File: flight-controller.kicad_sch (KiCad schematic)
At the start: 66 parts, among them J1 USB_C_Receptacle_USB2.0, Q1 AO3400A, SW1 SW_Push, U1 AT32F435RGT7, U2 BMI270, U3 BMP280, U4 W25N01GVZEIG, U5 AT7456E, U6 TPS54302, U7 TPS54302, U8 TLV75733PDBV, U9 USBLC6-2P6, Y1 27MHz

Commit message: Update notes and TODO items
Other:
- note added: "NOTES * TMR3 pins are for primary motors. * TMR3 pins could be mapped to TMR8. * TMR2/TMR9 are for servos. * Consider TagConnect for SWD * Some capacitors may be redundant depending on layout."
- note added: "TODO * Voltage sense * Pads * Connectors * LED resistors * OSD crystal"
- note removed: "NOTES * TMR3 pins are for primary motors. * TMR3 pins could be mapped to TMR8. * TMR2/TMR9 are for servos. * Confirm that crystal is not needed for USB. * Check we can interrupt on PB0 * LED supplies can be 5V as long as LED pins on MCU are FT. * Consider TagConnect for SWD"
- note removed: "TODO * Voltage sense * Current sense * Pads * Connectors"
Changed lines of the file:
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@@
     (effects (font (size 1.27 1.27)) (justify left bottom))
   )
-  (text "TODO\n* Voltage sense\n* Current sense\n* Pads\n* Connectors"
+  (text "TODO\n* Voltage sense\n* Pads\n* Connectors\n* LED resistors\n* OSD crystal"
     (at 264.16 109.22 0)
     (effects (font (size 1.27 1.27)) (justify left bottom))
   )
-  (text "NOTES\n* TMR3 pins are for primary motors.\n* TMR3 pins could be mapped to TMR8.\n* TMR2/TMR9 are for servos.\n* Confirm that crystal is not needed\n  for USB.\n* Check we can interrupt on PB0\n* LED supplies can be 5V as long as\n  LED pins on MCU are FT.\n* Consider TagConnect for SWD"
+  (text "NOTES\n* TMR3 pins are for primary motors.\n* TMR3 pins could be mapped to TMR8.\n* TMR2/TMR9 are for servos.\n* Consider TagConnect for SWD\n* Some capacitors may be redundant\n  depending on layout."
     (at 223.52 109.22 0)
     (effects (font (size 1.27 1.27)) (justify left bottom))

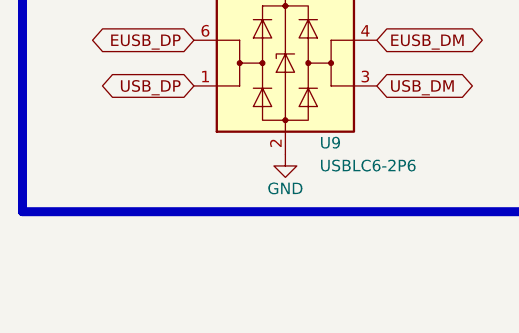
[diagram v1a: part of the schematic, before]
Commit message: Add 3D model for USB C, add speculative board and pad shapes
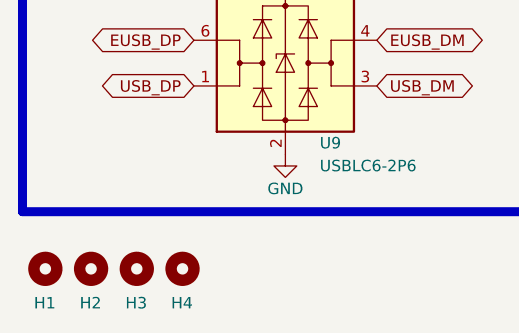
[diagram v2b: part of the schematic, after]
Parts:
- added H1, H2, H3, H4: MountingHole, MountingHole:MountingHole_3.2mm_M3, symbol Mechanical:MountingHole
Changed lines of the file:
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@@
+    )
+  )
+  (symbol (lib_id "Mechanical:MountingHole") (at 33.02 191.77 0) (unit 1)
+    (in_bom yes) (on_board yes) (dnp no)
+    (property "Reference" "H4" (at 31.75 195.58 0)
+      (effects (font (size 1.27 1.27)) (justify left))
+    )
+    (property "Value" "MountingHole" (at 35.56 193.675 0)
+      (effects (font (size 1.27 1.27)) (justify left) hide)
+    )
+    (property "Footprint" "MountingHole:MountingHole_3.2mm_M3" (at 33.02 191.77 0)
+      (effects (font (size 1.27 1.27)) hide)
+    )
+    (property "Datasheet" "~" (at 33.02 191.77 0)
+      (effects (font (size 1.27 1.27)) hide)
+    )
+    (instances
+      (project "flight-controller"
+        (path "/1ea4b7d2-6956-4f87-9f61-d89fdcbfe01f"
+          (reference "H4") (unit 1)
+        )
+      )
     )
   )
@@
         (path "/1ea4b7d2-6956-4f87-9f61-d89fdcbfe01f"
           (reference "#PWR015") (unit 1)
+        )
+      )
+    )
+  )
+  (symbol (lib_id "Mechanical:MountingHole") (at 27.94 191.77 0) (unit 1)
+    (in_bom yes) (on_board yes) (dnp no)
+    (property "Reference" "H3" (at 26.67 195.58 0)
+      (effects (font (size 1.27 1.27)) (justify left))
+    )
+    (property "Value" "MountingHole" (at 30.48 193.675 0)
+      (effects (font (size 1.27 1.27)) (justify left) hide)
+    )
+    (property "Footprint" "MountingHole:MountingHole_3.2mm_M3" (at 27.94 191.77 0)
+      (effects (font (size 1.27 1.27)) hide)
+    )
+    (property "Datasheet" "~" (at 27.94 191.77 0)
+      (effects (font (size 1.27 1.27)) hide)
+    )
+    (instances
+      (project "flight-controller"
+        (path "/1ea4b7d2-6956-4f87-9f61-d89fdcbfe01f"
+          (reference "H3") (unit 1)
         )
       )
@@
     )
   )
+  (symbol (lib_id "Mechanical:MountingHole") (at 17.78 191.77 0) (unit 1)
+    (in_bom yes) (on_board yes) (dnp no)
+    (property "Reference" "H1" (at 16.51 195.58 0)
+      (effects (font (size 1.27 1.27)) (justify left))
+    )
+    (property "Value" "MountingHole" (at 20.32 193.675 0)
+      (effects (font (size 1.27 1.27)) (justify left) hide)
+    )
+    (property "Footprint" "MountingHole:MountingHole_3.2mm_M3" (at 17.78 191.77 0)
+      (effects (font (size 1.27 1.27)) hide)
+    )
+    (property "Datasheet" "~" (at 17.78 191.77 0)
+      (effects (font (size 1.27 1.27)) hide)
+    )
+    (instances
+      (project "flight-controller"
+        (path "/1ea4b7d2-6956-4f87-9f61-d89fdcbfe01f"
+          (reference "H1") (unit 1)
+        )
+      )
+    )
+  )
   (symbol (lib_id "Transistor_FET:AO3400A") (at 203.2 100.33 0) (unit 1)
     (in_bom yes) (on_board yes) (dnp no) (fields_autoplaced)
@@
         )
       )
+    )
+  )
+  (symbol (lib_id "Mechanical:MountingHole") (at 22.86 191.77 0) (unit 1)
+    (in_bom yes) (on_board yes) (dnp no)
+    (property "Reference" "H2" (at 21.59 195.58 0)
+      (effects (font (size 1.27 1.27)) (justify left))
+    )
+    (property "Value" "MountingHole" (at 25.4 193.675 0)
+      (effects (font (size 1.27 1.27)) (justify left) hide)
+    )
+    (property "Footprint" "MountingHole:MountingHole_3.2mm_M3" (at 22.86 191.77 0)
+      (effects (font (size 1.27 1.27)) hide)
+    )
+    (property "Datasheet" "~" (at 22.86 191.77 0)
+      (effects (font (size 1.27 1.27)) hide)
+    )
+    (instances
+      (project "flight-controller"
+        (path "/1ea4b7d2-6956-4f87-9f61-d89fdcbfe01f"
+          (reference "H2") (unit 1)
+        )
+      )

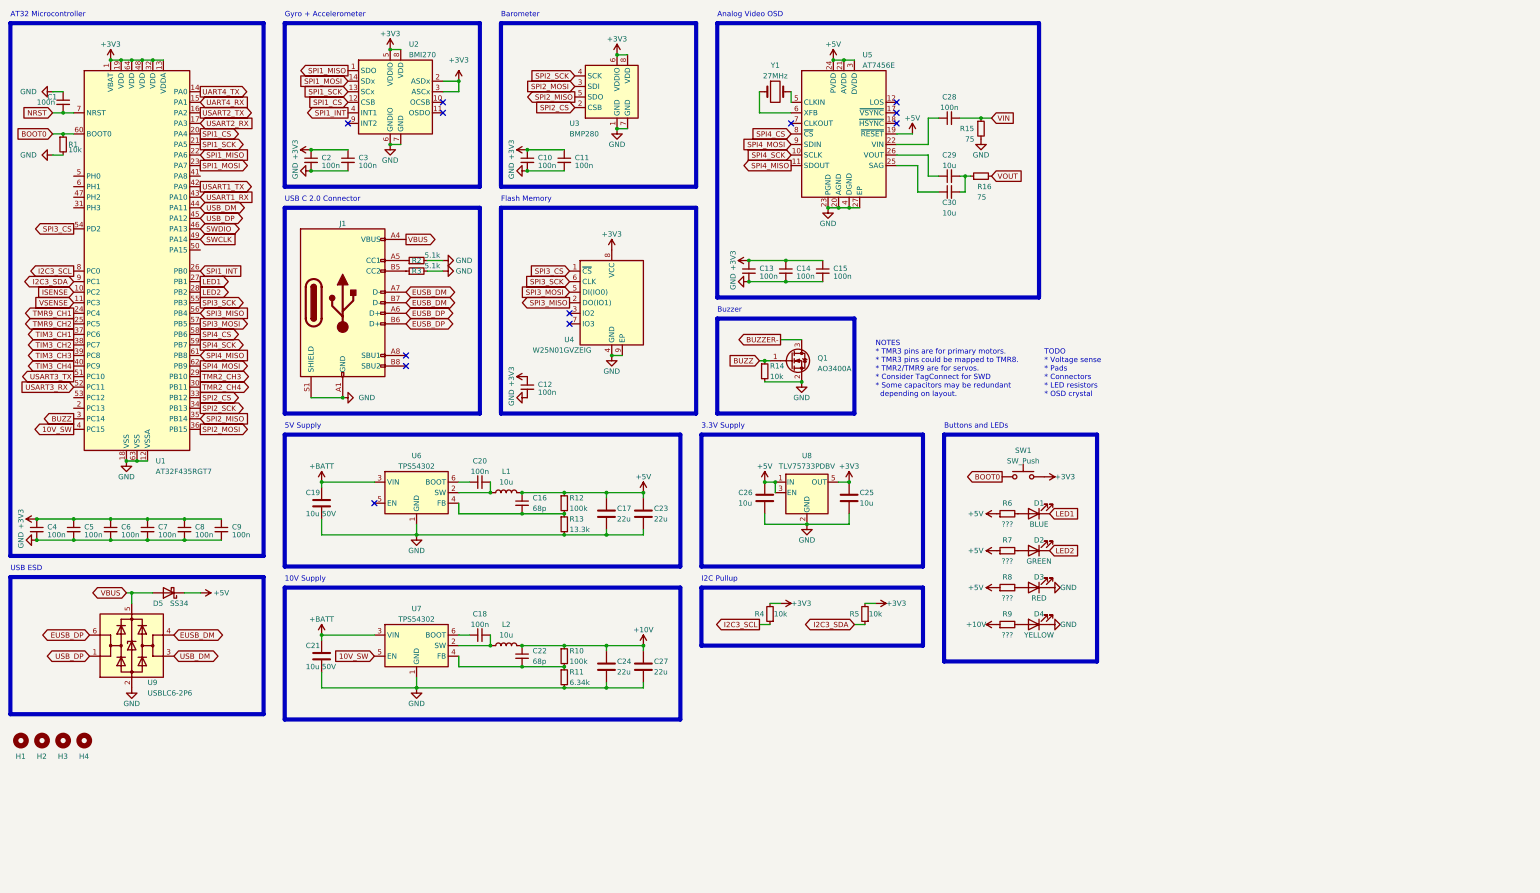
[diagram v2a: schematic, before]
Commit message: Add voltage sense divider, rework board shape
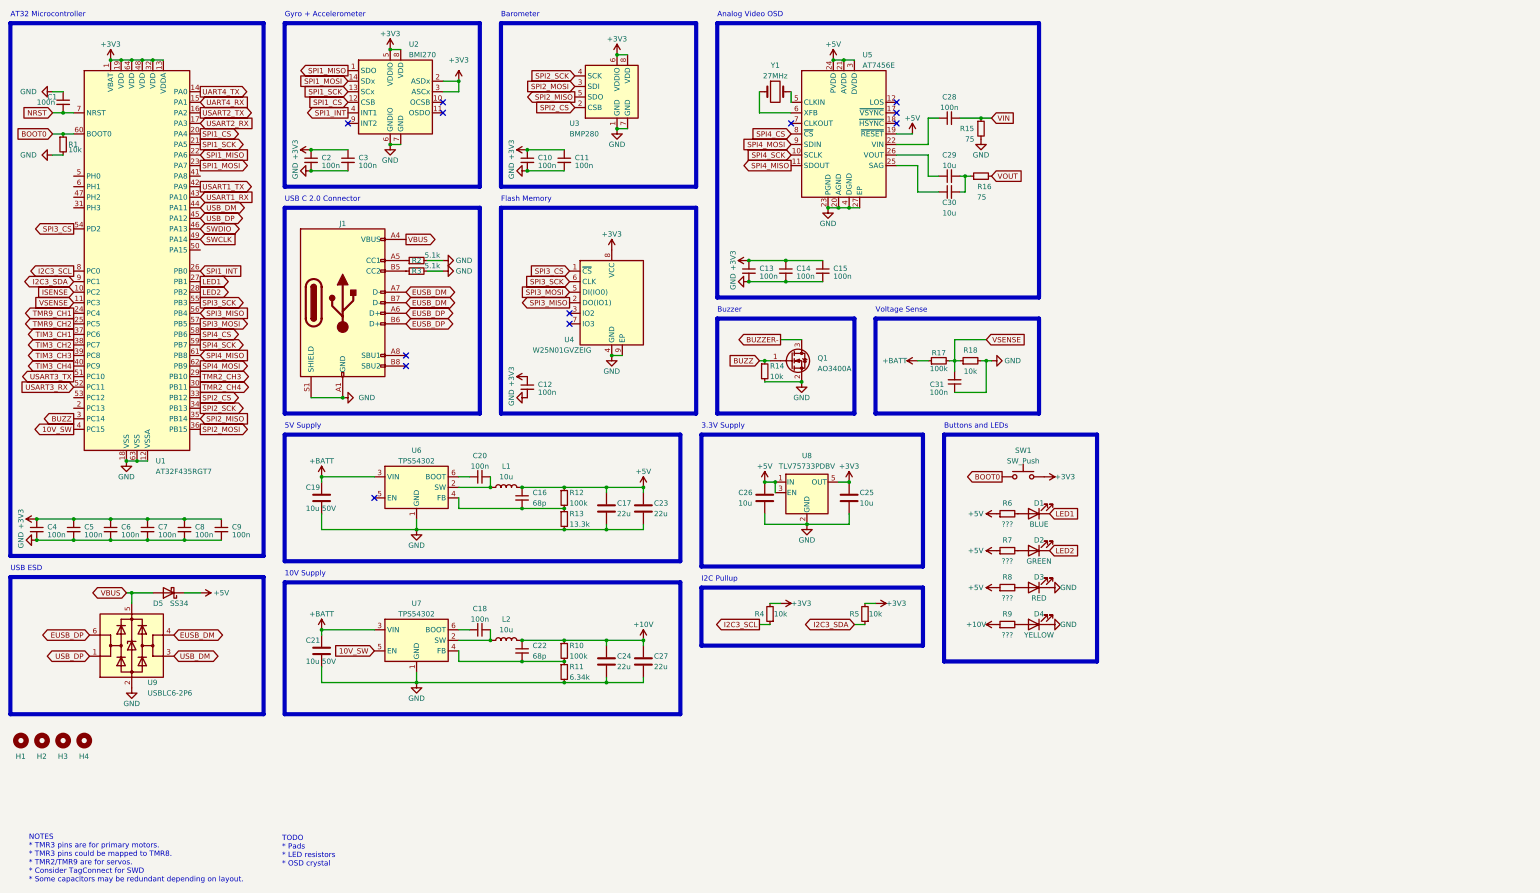
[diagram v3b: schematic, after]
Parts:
- added C31: 100n, Capacitor_SMD:C_0402_1005Metric, symbol Device:C_Small
- added R17: 100k, Resistor_SMD:R_0402_1005Metric, symbol Device:R_Small
- added R18: 10k, Resistor_SMD:R_0402_1005Metric, symbol Device:R_Small
- H1, H2, H3, H4: footprint MountingHole:MountingHole_3.2mm_M3 -> MountingHole:MountingHole_4mm
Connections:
- net +BATT: now also R17.1
- net GND: now also C31.1, R18.2
- net VSENSE: now also C31.2, R17.2, R18.1
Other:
- note added: "TODO * Pads * LED resistors * OSD crystal"
- note added: "Voltage Sense"
- note removed: "TODO * Voltage sense * Pads * Connectors * LED resistors * OSD crystal"
- moved on the sheet: C16, C17, C18, C19, C20, C21, C22, C23, C24, C27, L1, L2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

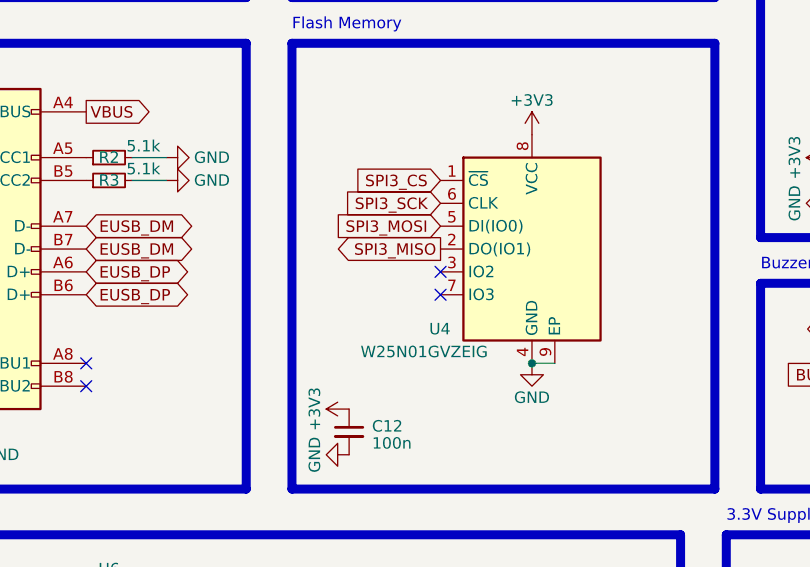
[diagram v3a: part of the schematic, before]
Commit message: Add missing HOLD and WP connections to flash
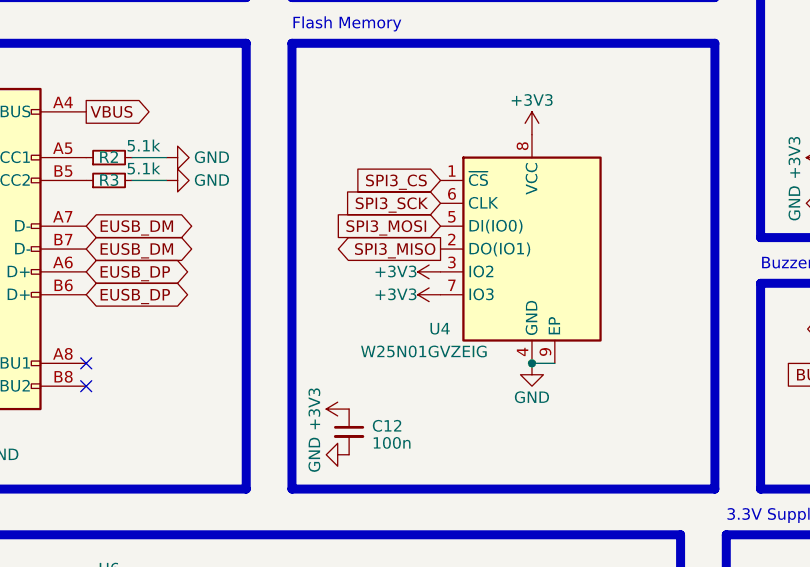
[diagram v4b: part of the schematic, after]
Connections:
- net +3V3: now also U4.3 (IO2), U4.7 (IO3)
- no-connect marks 12 -> 10
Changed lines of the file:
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@@
   (no_connect (at 110.49 101.6))
   (no_connect (at 110.49 99.06))
-  (no_connect (at 149.86 88.9))
   (no_connect (at 96.52 43.18))
-  (no_connect (at 149.86 91.44))
   (no_connect (at 102.87 133.35))
   (no_connect (at 119.38 40.64))
@@
     )
   )
+  (symbol (lib_id "power:+3V3") (at 149.86 91.44 90) (unit 1)
+    (in_bom yes) (on_board yes) (dnp no)
+    (property "Reference" "#PWR053" (at 153.67 91.44 0)
+      (effects (font (size 1.27 1.27)) hide)
+    )
+    (property "Value" "+3V3" (at 147.32 91.44 90)
+      (effects (font (size 1.27 1.27)) (justify left))
+    )
+    (property "Footprint" "" (at 149.86 91.44 0)
+      (effects (font (size 1.27 1.27)) hide)
+    )
+    (property "Datasheet" "" (at 149.86 91.44 0)
+      (effects (font (size 1.27 1.27)) hide)
+    )
+    (pin "1")
+    (instances
+      (project "flight-controller"
+        (path "/1ea4b7d2-6956-4f87-9f61-d89fdcbfe01f"
+          (reference "#PWR053") (unit 1)
+        )
+      )
+    )
+  )
   (symbol (lib_id "power:GND") (at 139.7 54.61 270) (unit 1)
     (in_bom yes) (on_board yes) (dnp no)
@@
         )
       )
+    )
+  )
+  (symbol (lib_id "power:+3V3") (at 149.86 88.9 90) (unit 1)
+    (in_bom yes) (on_board yes) (dnp no)
+    (property "Reference" "#PWR052" (at 153.67 88.9 0)
+      (effects (font (size 1.27 1.27)) hide)
+    )
+    (property "Value" "+3V3" (at 147.32 88.9 90)
+      (effects (font (size 1.27 1.27)) (justify left))
+    )
+    (property "Footprint" "" (at 149.86 88.9 0)
+      (effects (font (size 1.27 1.27)) hide)
+    )
+    (property "Datasheet" "" (at 149.86 88.9 0)
+      (effects (font (size 1.27 1.27)) hide)
+    )
+    (pin "1")
+    (instances
+      (project "flight-controller"
+        (path "/1ea4b7d2-6956-4f87-9f61-d89fdcbfe01f"
+          (reference "#PWR052") (unit 1)
+        )
+      )
